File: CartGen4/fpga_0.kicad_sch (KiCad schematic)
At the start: 12 parts, among them U9 LFXP2-8E-5MN132C

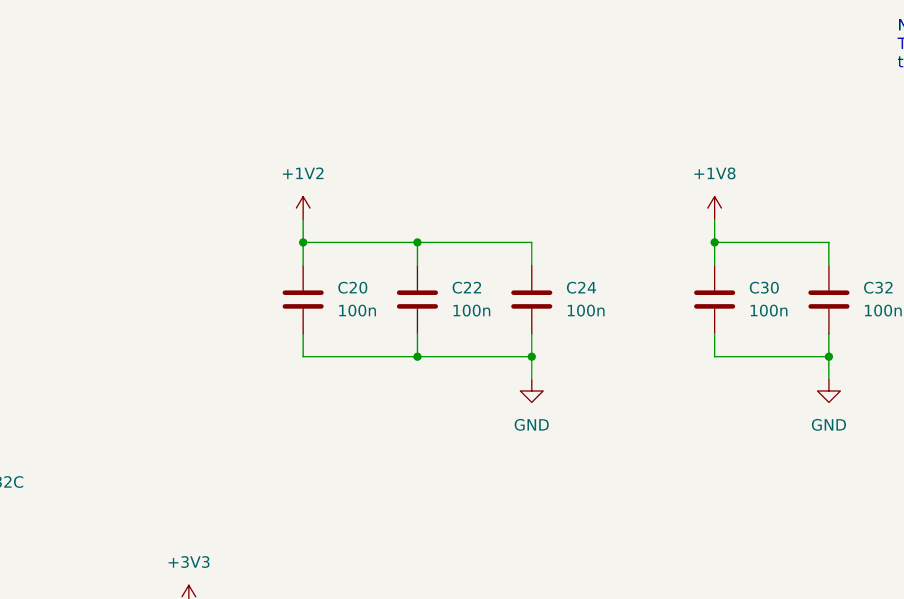
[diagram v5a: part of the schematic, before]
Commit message: Added decoupling capacitor to lone 1V8 pin
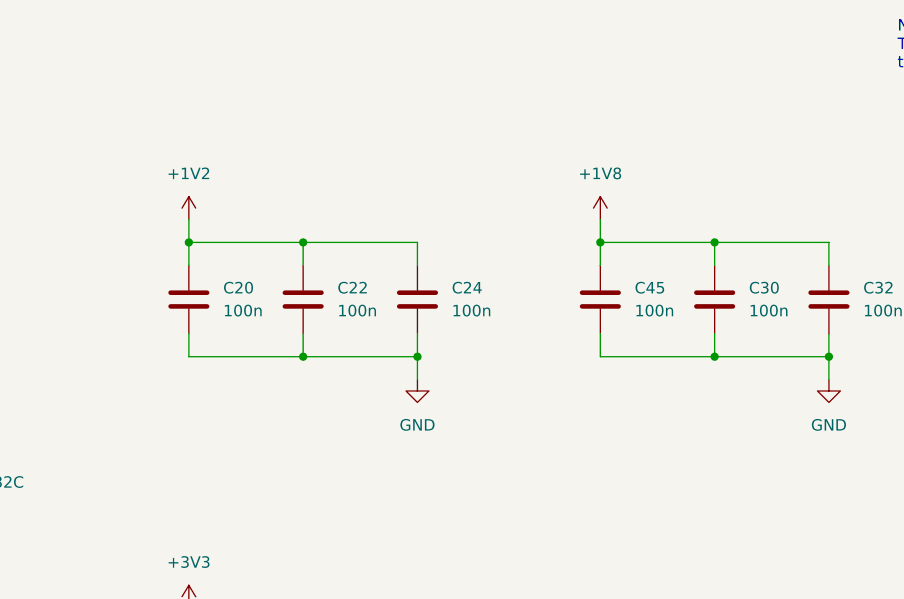
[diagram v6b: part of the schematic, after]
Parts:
- added C45: 100n, Capacitor_SMD:C_0402_1005Metric_Pad0.74x0.62mm_HandSolder, symbol Device:C
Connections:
- net +1V8: now also C45.1
- net GND: now also C45.2
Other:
- moved on the sheet: C20, C22, C24

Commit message: Minor adjustments
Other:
- note added: "This sheet contains connections to the FPGA. It contains the following: - PSRAM connections - General purpose signals - SPI bus - Clocking - JTAG connections"
- note removed: "This sheet contains connections to the FPGA. It contains the following: - PSRAM connections - Power - SPI bus - Clocking - JTAG connections"

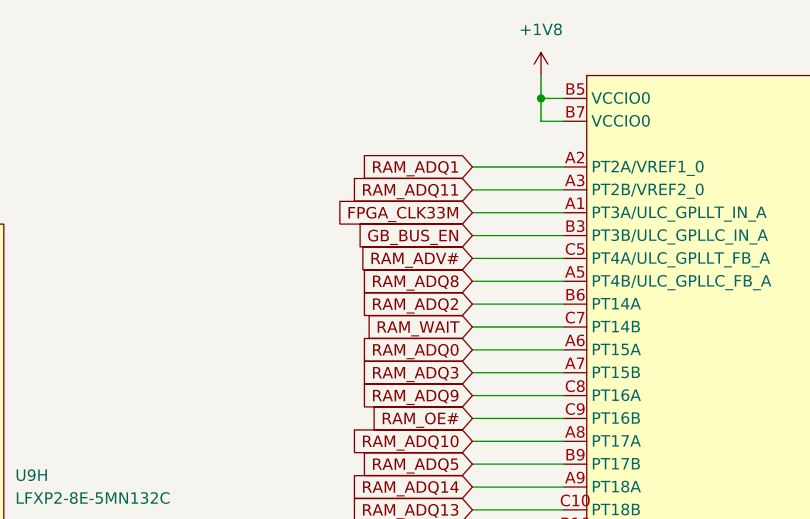
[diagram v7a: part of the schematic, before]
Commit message: Fixed GB_BUS_EN not being on 3V3 bank Added CLK_EN to ext clock
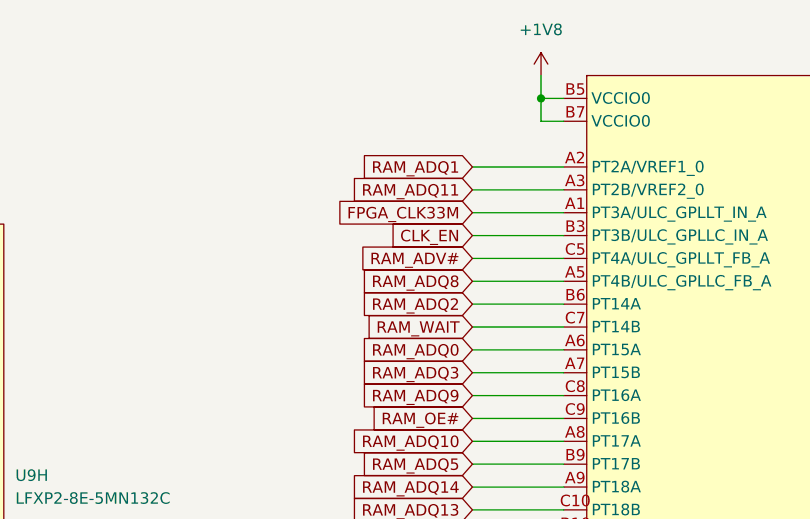
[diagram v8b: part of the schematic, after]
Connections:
- net GB_BUS_EN renamed CLK_EN
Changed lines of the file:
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@@
     )
   )
-  (global_label "GB_BUS_EN" (shape input) (at 135.89 45.72 180) (fields_autoplaced)
+  (global_label "CLK_EN" (shape input) (at 135.89 45.72 180) (fields_autoplaced)
     (effects (font (size 1.27 1.27)) (justify right))
-    (property "Intersheet References" "${INTERSHEET_REFS}" (id 0) (at 122.7121 45.6406 0)
+    (property "Intersheet References" "${INTERSHEET_REFS}" (id 0) (at 126.4617 45.6406 0)
       (effects (font (size 1.27 1.27)) (justify right) hide)
     )
